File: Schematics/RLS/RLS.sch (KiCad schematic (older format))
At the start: 24 parts, among them J6 ADS1115, U1 ARDUINO_MEGA_SHIELD

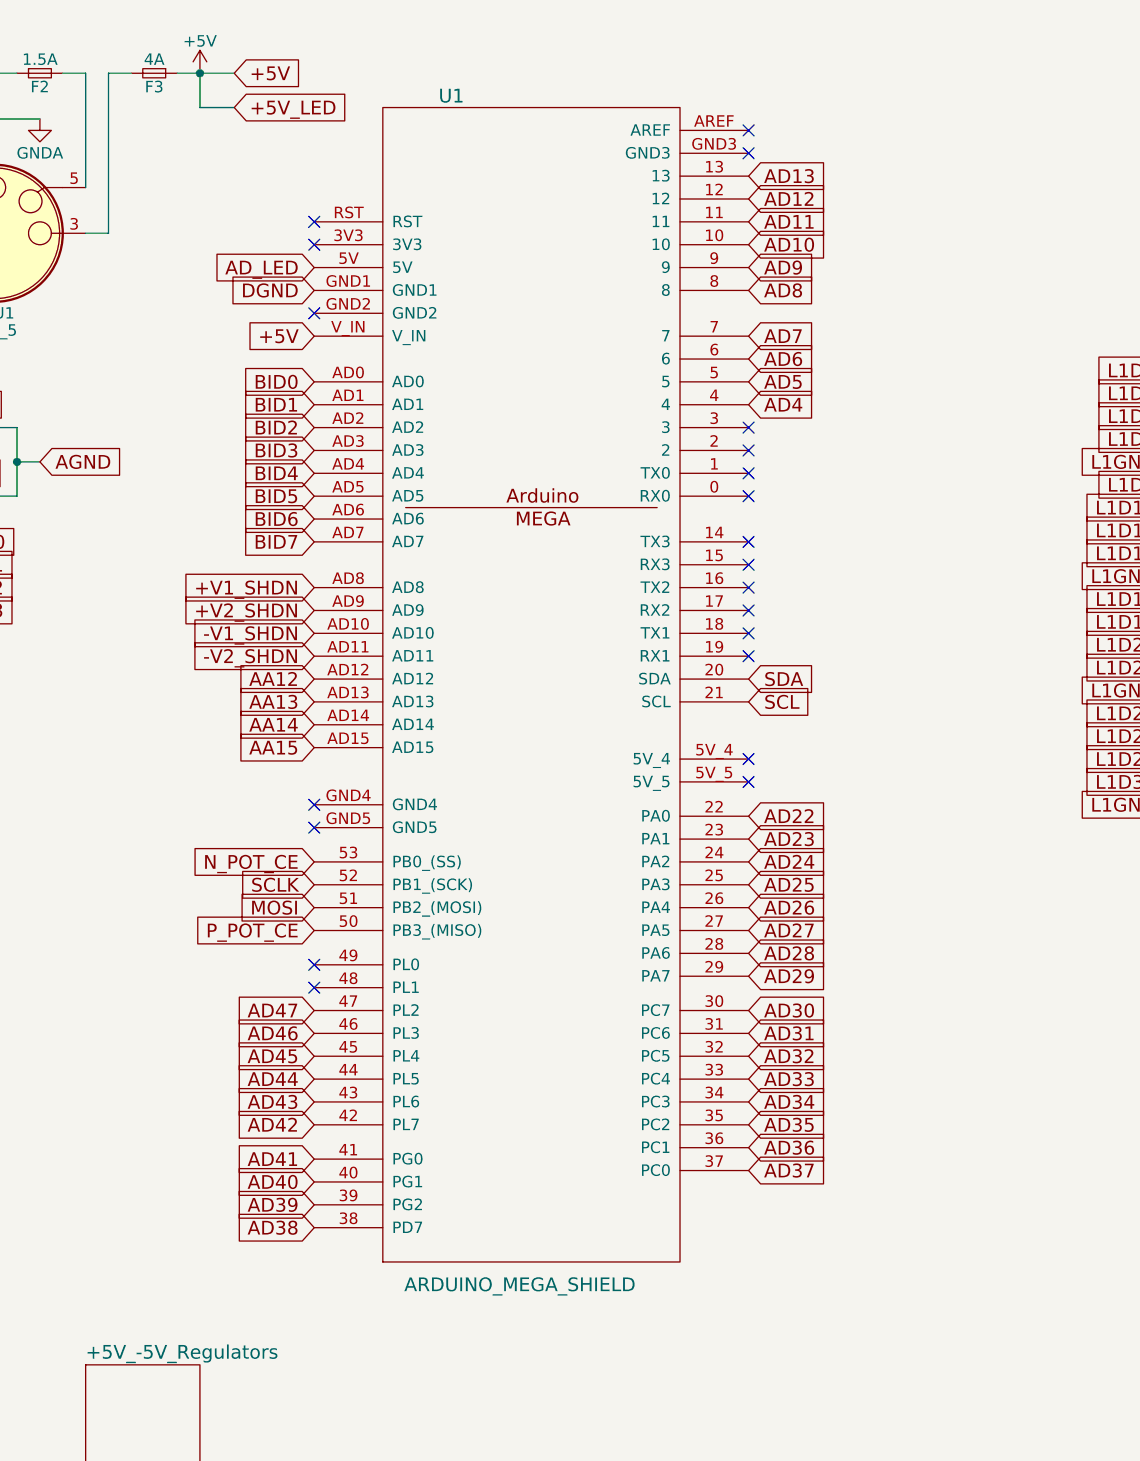
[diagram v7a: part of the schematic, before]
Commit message: Removed duplicate folder
Removing duplicate folder Andrew created. Merged the schematic folder back where it should be for RLS.
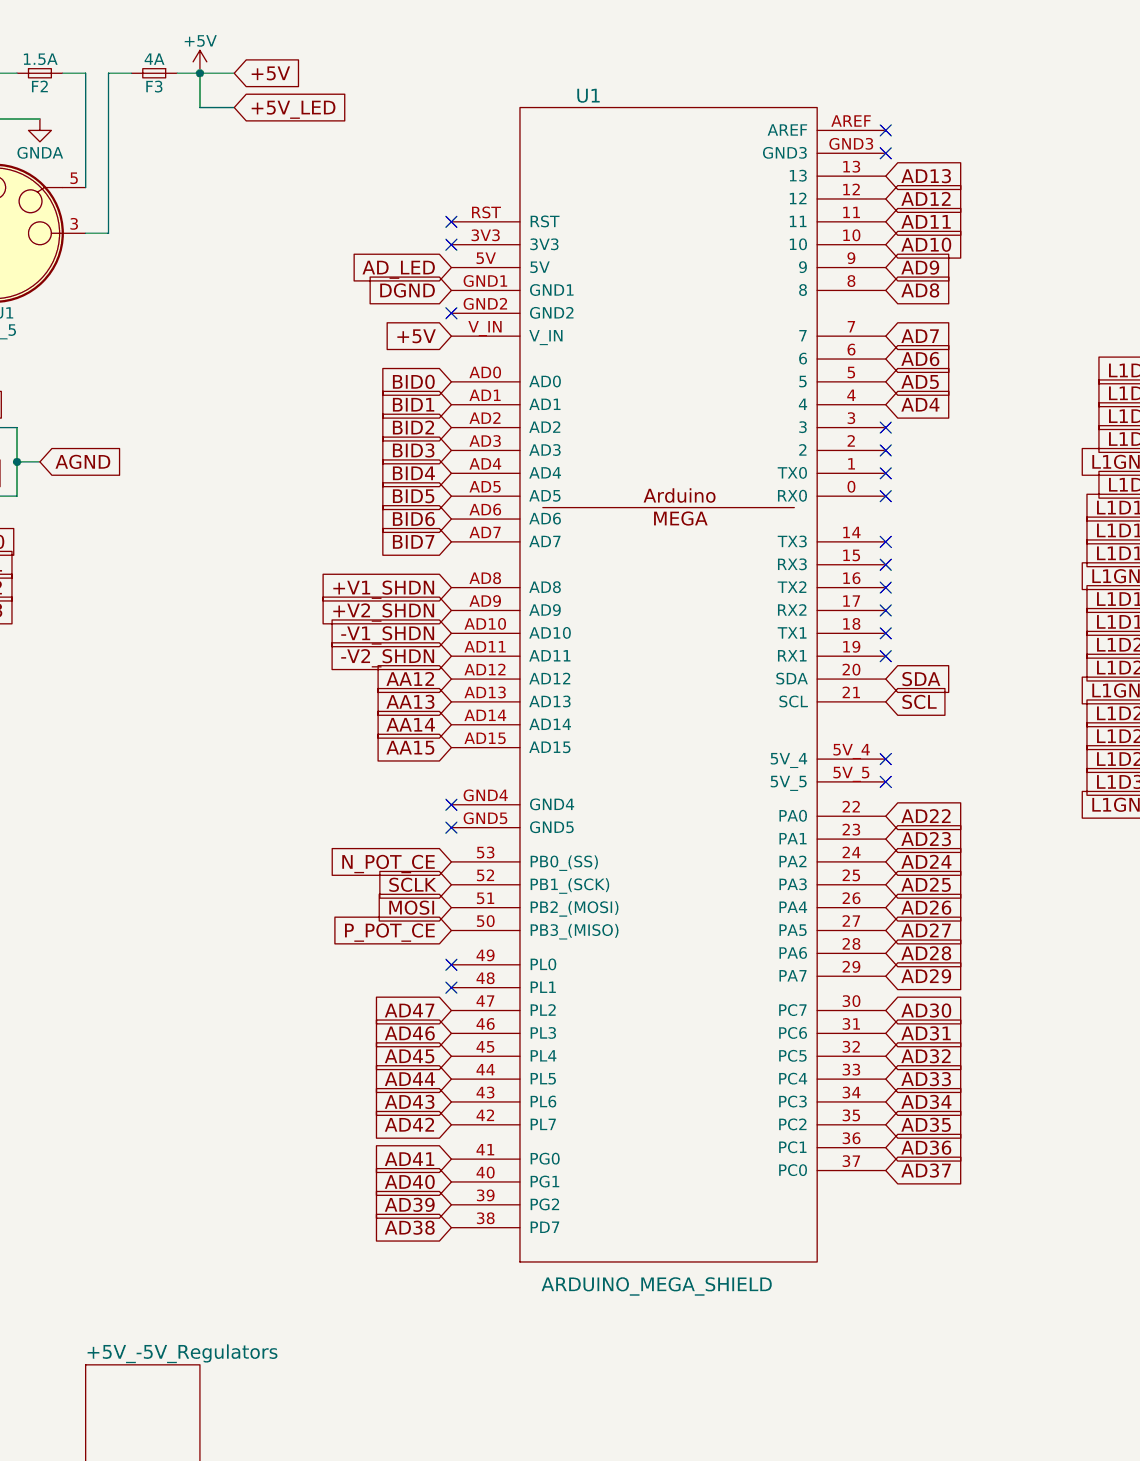
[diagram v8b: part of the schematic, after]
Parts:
- PSU1: footprint (none) -> RLS_CustomFootprints:Molex_2x3_3.5mm
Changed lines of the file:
@@
 LIBS:contrib
 LIBS:valves
+LIBS:arduino_shield
+LIBS:arduino_shieldsNCL
 LIBS:RLS-cache
 EELAYER 25 0
@@
 encoding utf-8
 Sheet 1 7
-Title ""
+Title "Remote Lab System"
 Date ""
 Rev ""
@@
 Text GLabel 7400 5100 3    60   Input ~ 0
 L2D0
-$Comp
-L ARDUINO_MEGA_SHIELD U1
-U 1 1 594ADDBF
-P 4150 3350
-F 0 "U1" H 3750 5850 60  0000 C CNN
-F 1 "ARDUINO_MEGA_SHIELD" H 4050 650 60  0000 C CNN
-F 2 "" H 4150 3350 60  0001 C CNN
-F 3 "" H 4150 3350 60  0001 C CNN
-	1    4150 3350
-	1    0    0    -1
-$EndComp
-Text GLabel 5050 2200 2    60   Input ~ 0
+Text GLabel 5650 2200 2    60   Input ~ 0
 AD4
-Text GLabel 5050 2100 2    60   Input ~ 0
+Text GLabel 5650 2100 2    60   Input ~ 0
 AD5
-Text GLabel 5050 2000 2    60   Input ~ 0
+Text GLabel 5650 2000 2    60   Input ~ 0
 AD6
-Text GLabel 5050 1900 2    60   Input ~ 0
+Text GLabel 5650 1900 2    60   Input ~ 0
 AD7
-Text GLabel 5050 1700 2    60   Input ~ 0
+Text GLabel 5650 1700 2    60   Input ~ 0
 AD8
-Text GLabel 5050 1600 2    60   Input ~ 0
+Text GLabel 5650 1600 2    60   Input ~ 0
 AD9
-Text GLabel 5050 1500 2    60   Input ~ 0
+Text GLabel 5650 1500 2    60   Input ~ 0
 AD10
-Text GLabel 5050 1400 2    60   Input ~ 0
+Text GLabel 5650 1400 2    60   Input ~ 0
 AD11
-Text GLabel 5050 1300 2    60   Input ~ 0
+Text GLabel 5650 1300 2    60   Input ~ 0
 AD12
-Text GLabel 5050 1200 2    60   Input ~ 0
+Text GLabel 5650 1200 2    60   Input ~ 0
 AD13
-Text GLabel 5050 4000 2    60   Input ~ 0
+Text GLabel 5650 4000 2    60   Input ~ 0
 AD22
-Text GLabel 5050 4100 2    60   Input ~ 0
+Text GLabel 5650 4100 2    60   Input ~ 0
 AD23
-Text GLabel 5050 4200 2    60   Input ~ 0
+Text GLabel 5650 4200 2    60   Input ~ 0
 AD24
-Text GLabel 5050 4300 2    60   Input ~ 0
+Text GLabel 5650 4300 2    60   Input ~ 0
 AD25
-Text GLabel 5050 4400 2    60   Input ~ 0
+Text GLabel 5650 4400 2    60   Input ~ 0
 AD26
-Text GLabel 5050 4500 2    60   Input ~ 0
+Text GLabel 5650 4500 2    60   Input ~ 0
 AD27
-Text GLabel 5050 4600 2    60   Input ~ 0
+Text GLabel 5650 4600 2    60   Input ~ 0
 AD28
-Text GLabel 5050 4700 2    60   Input ~ 0
+Text GLabel 5650 4700 2    60   Input ~ 0
 AD29
-Text GLabel 5050 4850 2    60   Input ~ 0
+Text GLabel 5650 4850 2    60   Input ~ 0
 AD30
-Text GLabel 5050 4950 2    60   Input ~ 0
+Text GLabel 5650 4950 2    60   Input ~ 0
 AD31
-Text GLabel 5050 5050 2    60   Input ~ 0
+Text GLabel 5650 5050 2    60   Input ~ 0
 AD32
-Text GLabel 5050 5150 2    60   Input ~ 0
+Text GLabel 5650 5150 2    60   Input ~ 0
 AD33
-Text GLabel 3150 5150 0    60   Input ~ 0
+Text GLabel 3750 5150 0    60   Input ~ 0
 AD44
-Text GLabel 5050 5250 2    60   Input ~ 0
+Text GLabel 5650 5250 2    60   Input ~ 0
 AD34
-Text GLabel 5050 5350 2    60   Input ~ 0
+Text GLabel 5650 5350 2    60   Input ~ 0
 AD35
-Text GLabel 5050 5450 2    60   Input ~ 0
+Text GLabel 5650 5450 2    60   Input ~ 0
 AD36
-Text GLabel 5050 5550 2    60   Input ~ 0
+Text GLabel 5650 5550 2    60   Input ~ 0
 AD37
-Text GLabel 3150 5800 0    60   Input ~ 0
+Text GLabel 3750 5800 0    60   Input ~ 0
 AD38
-Text GLabel 3150 5700 0    60   Input ~ 0
+Text GLabel 3750 5700 0    60   Input ~ 0
 AD39
-Text GLabel 3150 5600 0    60   Input ~ 0
+Text GLabel 3750 5600 0    60   Input ~ 0
 AD40
-Text GLabel 3150 5500 0    60   Input ~ 0
+Text GLabel 3750 5500 0    60   Input ~ 0
 AD41
-Text GLabel 3150 5350 0    60   Input ~ 0
+Text GLabel 3750 5350 0    60   Input ~ 0
 AD42
-Text GLabel 3150 5250 0    60   Input ~ 0
+Text GLabel 3750 5250 0    60   Input ~ 0
 AD43
-Text GLabel 3150 5050 0    60   Input ~ 0
+Text GLabel 3750 5050 0    60   Input ~ 0
 AD45
-Text GLabel 3150 4950 0    60   Input ~ 0
+Text GLabel 3750 4950 0    60   Input ~ 0
 AD46
-Text GLabel 3150 4850 0    60   Input ~ 0
+Text GLabel 3750 4850 0    60   Input ~ 0
 AD47
-Text GLabel 3150 2100 0    60   Input ~ 0
+Text GLabel 3750 2100 0    60   Input ~ 0
 BID0
-Text GLabel 3150 2200 0    60   Input ~ 0
+Text GLabel 3750 2200 0    60   Input ~ 0
 BID1
-Text GLabel 3150 2300 0    60   Input ~ 0
+Text GLabel 3750 2300 0    60   Input ~ 0
 BID2
-Text GLabel 3150 2400 0    60   Input ~ 0
+Text GLabel 3750 2400 0    60   Input ~ 0
 BID3
-Text GLabel 3150 2500 0    60   Input ~ 0
+Text GLabel 3750 2500 0    60   Input ~ 0
 BID4
-Text GLabel 3150 2600 0    60   Input ~ 0
+Text GLabel 3750 2600 0    60   Input ~ 0
 BID5
-Text GLabel 3150 2700 0    60   Input ~ 0
+Text GLabel 3750 2700 0    60   Input ~ 0
 BID6
-Text GLabel 3150 2800 0    60   Input ~ 0
+Text GLabel 3750 2800 0    60   Input ~ 0
 BID7
-Text GLabel 3150 3600 0    60   Input ~ 0
+Text GLabel 3750 3600 0    60   Input ~ 0
 AA14
-Text GLabel 3150 3700 0    60   Input ~ 0
+Text GLabel 3750 3700 0    60   Input ~ 0
 AA15
-NoConn ~ 5050 3750
-NoConn ~ 5050 3850
+NoConn ~ 5650 3750
+NoConn ~ 5650 3850
 $Comp
 L DIN_5-RESCUE-RLS PSU1
@@
 F 0 "PSU1" H 1750 1100 50  0000 C CNN
 F 1 "DIN_5" H 1750 1025 50  0000 C CNN
-F 2 "" H 1750 1450 50  0001 C CNN
+F 2 "RLS_CustomFootprints:Molex_2x3_3.5mm" H 1750 1450 50  0001 C CNN
 F 3 "" H 1750 1450 50  0001 C CNN
 	1    1750 1450
@@
 SDA
 NoConn ~ 1500 2700
-Text GLabel 5050 3400 2    60   Input ~ 0
+Text GLabel 5650 3400 2    60   Input ~ 0
 SDA
-Text GLabel 5050 3500 2    60   Input ~ 0
+Text GLabel 5650 3500 2    60   Input ~ 0
 SCL
-Text GLabel 3150 3400 0    60   Input ~ 0
+Text GLabel 3750 3400 0    60   Input ~ 0
 AA12
-Text GLabel 3150 3500 0    60   Input ~ 0
+Text GLabel 3750 3500 0    60   Input ~ 0
 AA13
 $Comp
@@
 F1 "Positive_Regulators.sch" 60
 $EndSheet
-Text GLabel 3150 4200 0    60   Input ~ 0
+Text GLabel 3750 4200 0    60   Input ~ 0
 N_POT_CE
-Text GLabel 3150 4500 0    60   Input ~ 0
+Text GLabel 3750 4500 0    60   Input ~ 0
 P_POT_CE
-Text GLabel 3150 4300 0    60   Input ~ 0
+Text GLabel 3750 4300 0    60   Input ~ 0
 SCLK
-Text GLabel 3150 4400 0    60   Input ~ 0
+Text GLabel 3750 4400 0    60   Input ~ 0
 MOSI
-Text GLabel 3150 3000 0    60   Input ~ 0
+Text GLabel 3750 3000 0    60   Input ~ 0
 +V1_SHDN
-Text GLabel 3150 3100 0    60   Input ~ 0
+Text GLabel 3750 3100 0    60   Input ~ 0
 +V2_SHDN
-Text GLabel 3150 3200 0    60   Input ~ 0
+Text GLabel 3750 3200 0    60   Input ~ 0
 -V1_SHDN
-Text GLabel 3150 3300 0    60   Input ~ 0
+Text GLabel 3750 3300 0    60   Input ~ 0
 -V2_SHDN
 $Sheet
@@
 F1 "+5V_-5V_Regulator.sch" 60
 $EndSheet
-NoConn ~ 3150 3950
-NoConn ~ 3150 4050
-NoConn ~ 3150 4650
-NoConn ~ 3150 4750
-NoConn ~ 3150 1800
-NoConn ~ 3150 1500
-NoConn ~ 3150 1400
-NoConn ~ 5050 1000
-NoConn ~ 5050 1100
+NoConn ~ 3750 3950
+NoConn ~ 3750 4050
+NoConn ~ 3750 4650
+NoConn ~ 3750 4750
+NoConn ~ 3750 1800
+NoConn ~ 3750 1500
+NoConn ~ 3750 1400
+NoConn ~ 5650 1000
+NoConn ~ 5650 1100
 $Sheet
 S 600  6400 500  500
@@
 F1 "Logic_Analyzer_Circuit.sch" 60
 $EndSheet
-NoConn ~ 5050 3300
-NoConn ~ 5050 3200
-NoConn ~ 5050 3100
-NoConn ~ 5050 3000
-NoConn ~ 5050 2900
-NoConn ~ 5050 2800
-NoConn ~ 5050 2600
-NoConn ~ 5050 2500
-NoConn ~ 5050 2400
-NoConn ~ 5050 2300
-Text GLabel 3150 1700 0    60   Input ~ 0
+NoConn ~ 5650 3300
+NoConn ~ 5650 3200
+NoConn ~ 5650 3100
+NoConn ~ 5650 3000
+NoConn ~ 5650 2900
+NoConn ~ 5650 2800
+NoConn ~ 5650 2600
+NoConn ~ 5650 2500
+NoConn ~ 5650 2400
+NoConn ~ 5650 2300
+Text GLabel 3750 1700 0    60   Input ~ 0
 DGND
-Text GLabel 3150 1900 0    60   Input ~ 0
+Text GLabel 3750 1900 0    60   Input ~ 0
 +5V
 Wire Wire Line
@@
 	1    0    0    -1
 $EndComp
-Text GLabel 3150 1600 0    60   Input ~ 0
+Text GLabel 3750 1600 0    60   Input ~ 0
 AD_LED
 Text GLabel 1200 3900 1    60   Input ~ 0
@@
 Wire Wire Line
 	1650 3900 1650 3950
+$Comp
+L ARDUINO_MEGA_SHIELD U1
+U 1 1 595F5E81
+P 4750 3350
+F 0 "U1" H 4350 5850 60  0000 C CNN
+F 1 "ARDUINO_MEGA_SHIELD" H 4650 650 60  0000 C CNN
+F 2 "" H 4750 3350 60  0001 C CNN
+F 3 "" H 4750 3350 60  0001 C CNN
+	1    4750 3350
+	1    0    0    -1
+$EndComp
 $EndSCHEMATC
